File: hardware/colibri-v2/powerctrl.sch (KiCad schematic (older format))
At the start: 47 parts, among them CN1 XT60-M, CN2 XT60-F, CON1 BARREL_JACK, Q1 PDTC123JU, Q10 PDTC123JU, Q11 PDTA123JU, Q2 PDTA123JU, Q3 BSS138PW, Q4 FDMA530PZ, Q5 BSS138PW, Q6 BSS138PW, Q7 BSS138PW, Q8 AP6681GMT-HF-3TR, Q9 FDMA530PZ, SW10 B3F-1020, SW9 ALPS-SPPJ320600, T1 BATCHARGE+, T2 BATCHARGE-

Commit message: Adding and assigning footprints
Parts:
- Q3, Q5, Q6, Q7: footprint (none) -> TO_SOT_Packages_SMD:SOT-323
- Q4, Q9: footprint (none) -> Sigmadrone:FDMA530PZ
- SW10: value B3F-1020 -> OMRON B3F-1070; footprint (none) -> Sigmadrone:SW_TH_Tactile_Omron_B3F-10xx_6x6
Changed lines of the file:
@@
 F 0 "Q5" H 5600 2000 50  0000 R CNN
 F 1 "BSS138PW" H 5300 2150 50  0000 R CNN
-F 2 "" H 5500 2050 29  0001 C CNN
+F 2 "TO_SOT_Packages_SMD:SOT-323" H 5500 2050 29  0001 C CNN
 F 3 "" H 5300 1950 60  0000 C CNN
 	1    5300 1950
@@
 F 0 "Q9" H 7510 3260 50  0000 R CNN
 F 1 "FDMA530PZ" V 8000 3150 50  0000 R CNN
-F 2 "" H 7850 3250 29  0001 C CNN
+F 2 "Sigmadrone:FDMA530PZ" H 7850 3250 29  0001 C CNN
 F 3 "" H 7650 3150 60  0000 C CNN
 	1    7650 3150
@@
 F 0 "Q4" H 4060 3260 50  0000 R CNN
 F 1 "FDMA530PZ" V 4500 3150 50  0000 R CNN
-F 2 "" H 4400 3250 29  0001 C CNN
+F 2 "Sigmadrone:FDMA530PZ" H 4400 3250 29  0001 C CNN
 F 3 "" H 4200 3150 60  0000 C CNN
 	1    4200 3150
@@
 F 0 "Q6" H 6000 5050 50  0000 R CNN
 F 1 "BSS138PW" H 5700 5200 50  0000 R CNN
-F 2 "" H 5900 5100 29  0001 C CNN
+F 2 "TO_SOT_Packages_SMD:SOT-323" H 5900 5100 29  0001 C CNN
 F 3 "" H 5700 5000 60  0000 C CNN
 	1    5700 5000
@@
 F 0 "Q7" H 6650 5050 50  0000 R CNN
 F 1 "BSS138PW" H 6350 5200 50  0000 R CNN
-F 2 "" H 6550 5100 29  0001 C CNN
+F 2 "TO_SOT_Packages_SMD:SOT-323" H 6550 5100 29  0001 C CNN
 F 3 "" H 6350 5000 60  0000 C CNN
 	1    6350 5000
@@
 P 7750 5150
 F 0 "SW10" H 7900 5260 50  0000 C CNN
-F 1 "B3F-1020" H 7750 4950 50  0000 C CNN
-F 2 "" H 7750 5150 60  0001 C CNN
+F 1 "OMRON B3F-1070" H 7750 4950 50  0000 C CNN
+F 2 "Sigmadrone:SW_TH_Tactile_Omron_B3F-10xx_6x6" H 7750 5150 60  0001 C CNN
 F 3 "" H 7750 5150 60  0000 C CNN
 F 4 "1960939" H 7750 5150 60  0001 C CNN "Part"
@@
 F 0 "Q3" H 3750 6300 50  0000 R CNN
 F 1 "BSS138PW" H 3450 6450 50  0000 R CNN
-F 2 "" H 3650 6350 29  0001 C CNN
+F 2 "TO_SOT_Packages_SMD:SOT-323" H 3650 6350 29  0001 C CNN
 F 3 "" H 3450 6250 60  0000 C CNN
 	1    3450 6250

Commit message: Added footprints
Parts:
- removed D4: BZV55-C18, symbol ZENER
- removed Q1: PDTC123JU, TO_SOT_Packages_SMD:SOT-323, symbol RET_NPN_SMT
- removed Q2: PDTA123JU, TO_SOT_Packages_SMD:SOT-323, symbol RET_PNP_SMT
- added C125: 100nF/50V/X7R, Capacitors_SMD:C_0603, symbol C_SMT
- added U27: LTC4412, Sigmadrone:SOT23-6_LTC4412, symbol LTC4412
- D2: value D_Schottky -> VS-15MQ040NTRPBF; footprint (none) -> Sigmadrone:DO-214AC; Part (none) -> 1463215; Provider (none) -> Farnell
- D3, D8, D9: footprint (none) -> Diodes_SMD:SOD-323
- D5: footprint (none) -> Sigmadrone:DO-214AC
- D6, D7: footprint (none) -> Sigmadrone:SOD-80
- R43: value 10K/5% -> 100R/5%; Part 9331700 -> 9331689
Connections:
- wire segments 136 -> 138
- no-connect marks 0 -> 1

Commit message: Added Power Jack footprint
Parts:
- removed T1: BATCHARGE+, symbol 726386-2
- removed T2: BATCHARGE-, symbol 726386-2
- added CN12: XT60-F, Sigmadrone:xt60, symbol XT60
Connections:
- wire segments 138 -> 135
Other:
- moved on the sheet: C125, C26, C27, C28, C29, CN1, CN2, CON1, D2, D3, D5, D6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

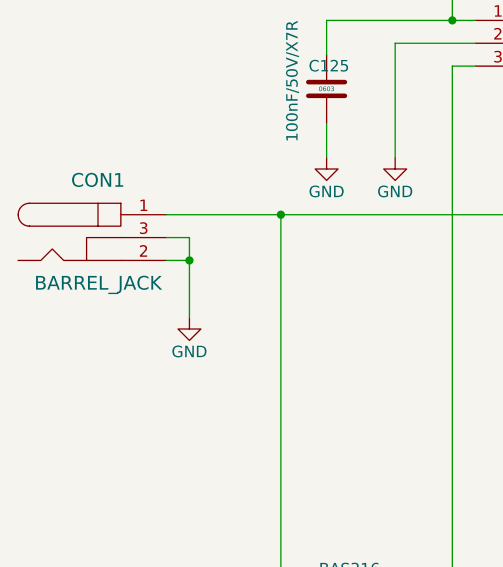
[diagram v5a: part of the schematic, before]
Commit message: Added footprints
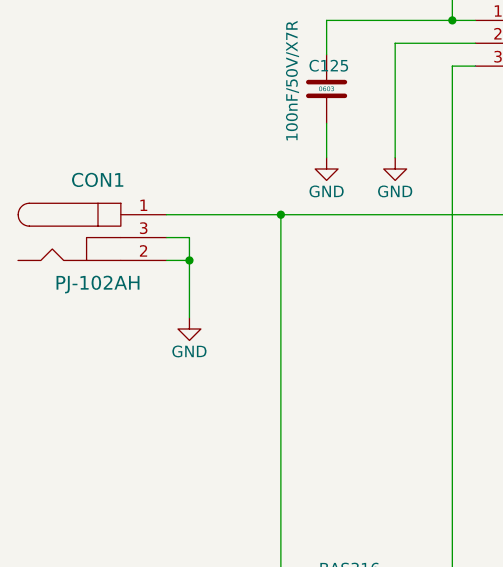
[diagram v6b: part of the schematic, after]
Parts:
- CON1: value BARREL_JACK -> PJ-102AH; footprint (none) -> Sigmadrone:PJ-102AH; Part (none) -> CP-102AH-ND; Provider (none) -> Digikey
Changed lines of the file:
@@
 $EndComp
 $Comp
-L +BATT #PWR49
+L +BATT #PWR051
 U 1 1 55962B26
 P 1650 950
-F 0 "#PWR49" H 1650 800 50  0001 C CNN
+F 0 "#PWR051" H 1650 800 50  0001 C CNN
 F 1 "+BATT" H 1650 1090 50  0000 C CNN
 F 2 "" H 1650 950 60  0000 C CNN
@@
 VH_CTRL
 $Comp
-L GND #PWR60
+L GND #PWR052
 U 1 1 55A491DA
 P 4850 2550
-F 0 "#PWR60" H 4850 2300 50  0001 C CNN
+F 0 "#PWR052" H 4850 2300 50  0001 C CNN
 F 1 "GND" H 4850 2400 50  0000 C CNN
 F 2 "" H 4850 2550 60  0000 C CNN
@@
 $EndComp
 $Comp
-L GND #PWR62
+L GND #PWR053
 U 1 1 55ADC831
 P 5400 2550
-F 0 "#PWR62" H 5400 2300 50  0001 C CNN
+F 0 "#PWR053" H 5400 2300 50  0001 C CNN
 F 1 "GND" H 5400 2400 50  0000 C CNN
 F 2 "" H 5400 2550 60  0000 C CNN
@@
 $EndComp
 $Comp
-L +BATT #PWR51
+L +BATT #PWR054
 U 1 1 55ADD6AC
 P 1650 3000
-F 0 "#PWR51" H 1650 2850 50  0001 C CNN
+F 0 "#PWR054" H 1650 2850 50  0001 C CNN
 F 1 "+BATT" H 1650 3140 50  0000 C CNN
 F 2 "" H 1650 3000 60  0000 C CNN
@@
 P 1000 4850
 F 0 "CON1" H 1000 5100 60  0000 C CNN
-F 1 "BARREL_JACK" H 1000 4650 60  0000 C CNN
-F 2 "" H 1000 4850 60  0001 C CNN
+F 1 "PJ-102AH" H 1000 4650 60  0000 C CNN
+F 2 "Sigmadrone:PJ-102AH" H 1000 4850 60  0001 C CNN
 F 3 "" H 1000 4850 60  0000 C CNN
+F 4 "CP-102AH-ND" H 1000 4850 60  0001 C CNN "Part"
+F 5 "Digikey" H 1000 4850 60  0001 C CNN "Provider"
 	1    1000 4850
 	1    0    0    -1
@@
 $EndComp
 $Comp
-L GND #PWR59
+L GND #PWR055
 U 1 1 564AD1EF
 P 3700 4450
-F 0 "#PWR59" H 3700 4200 50  0001 C CNN
+F 0 "#PWR055" H 3700 4200 50  0001 C CNN
 F 1 "GND" H 3700 4300 50  0000 C CNN
 F 2 "" H 3700 4450 60  0000 C CNN
@@
 $EndComp
 $Comp
-L GND #PWR65
+L GND #PWR056
 U 1 1 565060C5
 P 5800 5800
-F 0 "#PWR65" H 5800 5550 50  0001 C CNN
+F 0 "#PWR056" H 5800 5550 50  0001 C CNN
 F 1 "GND" H 5800 5650 50  0000 C CNN
 F 2 "" H 5800 5800 60  0000 C CNN
@@
 $EndComp
 $Comp
-L GND #PWR66
+L GND #PWR057
 U 1 1 565061BE
 P 6250 5800
-F 0 "#PWR66" H 6250 5550 50  0001 C CNN
+F 0 "#PWR057" H 6250 5550 50  0001 C CNN
 F 1 "GND" H 6250 5650 50  0000 C CNN
 F 2 "" H 6250 5800 60  0000 C CNN
@@
 $EndComp
 $Comp
-L GND #PWR67
+L GND #PWR058
 U 1 1 565065E3
 P 6650 5800
-F 0 "#PWR67" H 6650 5550 50  0001 C CNN
+F 0 "#PWR058" H 6650 5550 50  0001 C CNN
 F 1 "GND" H 6650 5650 50  0000 C CNN
 F 2 "" H 6650 5800 60  0000 C CNN
@@
 $EndComp
 $Comp
-L GND #PWR63
+L GND #PWR059
 U 1 1 56507987
 P 5400 5800
-F 0 "#PWR63" H 5400 5550 50  0001 C CNN
+F 0 "#PWR059" H 5400 5550 50  0001 C CNN
 F 1 "GND" H 5400 5650 50  0000 C CNN
 F 2 "" H 5400 5800 60  0000 C CNN
@@
 $EndComp
 $Comp
-L GND #PWR68
+L GND #PWR060
 U 1 1 5650962F
 P 7650 5800
-F 0 "#PWR68" H 7650 5550 50  0001 C CNN
+F 0 "#PWR060" H 7650 5550 50  0001 C CNN
 F 1 "GND" H 7650 5650 50  0000 C CNN
 F 2 "" H 7650 5800 60  0000 C CNN
@@
 $EndComp
 $Comp
-L +3V3 #PWR72
+L +3V3 #PWR061
 U 1 1 5650D441
 P 8800 4200
-F 0 "#PWR72" H 8800 4050 50  0001 C CNN
+F 0 "#PWR061" H 8800 4050 50  0001 C CNN
 F 1 "+3V3" H 8800 4340 50  0000 C CNN
 F 2 "" H 8800 4200 60  0000 C CNN
@@
 $EndComp
 $Comp
-L GND #PWR69
+L GND #PWR062
 U 1 1 5650DE62
 P 8200 3850
-F 0 "#PWR69" H 8200 3600 50  0001 C CNN
+F 0 "#PWR062" H 8200 3600 50  0001 C CNN
 F 1 "GND" H 8200 3700 50  0000 C CNN
 F 2 "" H 8200 3850 60  0000 C CNN
@@
 $EndComp
 $Comp
-L GND #PWR58
+L GND #PWR063
 U 1 1 5650ECED
 P 3550 7450
-F 0 "#PWR58" H 3550 7200 50  0001 C CNN
+F 0 "#PWR063" H 3550 7200 50  0001 C CNN
 F 1 "GND" H 3550 7300 50  0000 C CNN
 F 2 "" H 3550 7450 60  0000 C CNN
@@
 $EndComp
 $Comp
-L GND #PWR56
+L GND #PWR064
 U 1 1 5650ECF4
 P 3150 7450
-F 0 "#PWR56" H 3150 7200 50  0001 C CNN
+F 0 "#PWR064" H 3150 7200 50  0001 C CNN
 F 1 "GND" H 3150 7300 50  0000 C CNN
 F 2 "" H 3150 7450 60  0000 C CNN
@@
 $EndComp
 $Comp
-L +3V3 #PWR57
+L +3V3 #PWR065
 U 1 1 5650F275
 P 3550 5600
-F 0 "#PWR57" H 3550 5450 50  0001 C CNN
+F 0 "#PWR065" H 3550 5450 50  0001 C CNN
 F 1 "+3V3" H 3550 5740 50  0000 C CNN
 F 2 "" H 3550 5600 60  0000 C CNN
@@
 JTAG_PWR_ON
 $Comp
-L GND #PWR54
+L GND #PWR066
 U 1 1 56510E0B
 P 2300 4500
-F 0 "#PWR54" H 2300 4250 50  0001 C CNN
+F 0 "#PWR066" H 2300 4250 50  0001 C CNN
 F 1 "GND" H 2300 4350 50  0000 C CNN
 F 2 "" H 2300 4500 60  0000 C CNN
@@
 $EndComp
 $Comp
-L GND #PWR61
+L GND #PWR067
 U 1 1 5651137E
 P 5150 4000
-F 0 "#PWR61" H 5150 3750 50  0001 C CNN
+F 0 "#PWR067" H 5150 3750 50  0001 C CNN
 F 1 "GND" H 5150 3850 50  0000 C CNN
 F 2 "" H 5150 4000 60  0000 C CNN
@@
 $EndComp
 $Comp
-L GND #PWR64
+L GND #PWR068
 U 1 1 56511422
 P 5550 4000
-F 0 "#PWR64" H 5550 3750 50  0001 C CNN
+F 0 "#PWR068" H 5550 3750 50  0001 C CNN
 F 1 "GND" H 5550 3850 50  0000 C CNN
 F 2 "" H 5550 4000 60  0000 C CNN
@@
 $EndComp
 $Comp
-L GND #PWR50
+L GND #PWR069
 U 1 1 5651558E
 P 1650 1650
-F 0 "#PWR50" H 1650 1400 50  0001 C CNN
+F 0 "#PWR069" H 1650 1400 50  0001 C CNN
 F 1 "GND" H 1650 1500 50  0000 C CNN
 F 2 "" H 1650 1650 60  0000 C CNN
@@
 $EndComp
 $Comp
-L GND #PWR71
+L GND #PWR070
 U 1 1 56515698
 P 8250 1650
-F 0 "#PWR71" H 8250 1400 50  0001 C CNN
+F 0 "#PWR070" H 8250 1400 50  0001 C CNN
 F 1 "GND" H 8250 1500 50  0000 C CNN
 F 2 "" H 8250 1650 60  0000 C CNN
@@
 $EndComp
 $Comp
-L GND #PWR48
+L GND #PWR071
 U 1 1 5651D821
 P 1400 5200
-F 0 "#PWR48" H 1400 4950 50  0001 C CNN
+F 0 "#PWR071" H 1400 4950 50  0001 C CNN
 F 1 "GND" H 1400 5050 50  0000 C CNN
 F 2 "" H 1400 5200 60  0000 C CNN
@@
 $EndComp
 $Comp
-L GND #PWR52
+L GND #PWR072
 U 1 1 56520674
 P 1800 7450
-F 0 "#PWR52" H 1800 7200 50  0001 C CNN
+F 0 "#PWR072" H 1800 7200 50  0001 C CNN
 F 1 "GND" H 1800 7300 50  0000 C CNN
 F 2 "" H 1800 7450 60  0000 C CNN
@@
 $EndComp
 $Comp
-L GND #PWR75
+L GND #PWR073
 U 1 1 56522BEE
 P 9700 2600
-F 0 "#PWR75" H 9700 2350 50  0001 C CNN
+F 0 "#PWR073" H 9700 2350 50  0001 C CNN
 F 1 "GND" H 9700 2450 50  0000 C CNN
 F 2 "" H 9700 2600 60  0000 C CNN
@@
 $EndComp
 $Comp
-L +BATT #PWR74
+L +BATT #PWR074
 U 1 1 56523199
 P 9700 1450
-F 0 "#PWR74" H 9700 1300 50  0001 C CNN
+F 0 "#PWR074" H 9700 1300 50  0001 C CNN
 F 1 "+BATT" H 9700 1590 50  0000 C CNN
 F 2 "" H 9700 1450 60  0000 C CNN
@@
 $EndComp
 $Comp
-L GND #PWR73
+L GND #PWR075
 U 1 1 56523CCD
 P 9300 2600
-F 0 "#PWR73" H 9300 2350 50  0001 C CNN
+F 0 "#PWR075" H 9300 2350 50  0001 C CNN
 F 1 "GND" H 9300 2450 50  0000 C CNN
 F 2 "" H 9300 2600 60  0000 C CNN
@@
 $EndComp
 $Comp
-L GND #PWR76
+L GND #PWR076
 U 1 1 56524360
 P 10100 2600
-F 0 "#PWR76" H 10100 2350 50  0001 C CNN
+F 0 "#PWR076" H 10100 2350 50  0001 C CNN
 F 1 "GND" H 10100 2450 50  0000 C CNN
 F 2 "" H 10100 2600 60  0000 C CNN
@@
 $EndComp
 $Comp
-L VH #PWR70
+L VH #PWR077
 U 1 1 56C841E3
 P 8250 950
-F 0 "#PWR70" H 8250 800 50  0001 C CNN
+F 0 "#PWR077" H 8250 800 50  0001 C CNN
 F 1 "VH" H 8268 1124 50  0000 C CNN
 F 2 "" H 8250 950 50  0000 C CNN
@@
 $EndComp
 $Comp
-L PWR_FLAG #FLG4
+L PWR_FLAG #FLG078
 U 1 1 56CCA634
 P 2050 950
-F 0 "#FLG4" H 2050 1045 50  0001 C CNN
+F 0 "#FLG078" H 2050 1045 50  0001 C CNN
 F 1 "PWR_FLAG" H 2050 1174 50  0000 C CNN
 F 2 "" H 2050 950 50  0000 C CNN
@@
 $EndComp
 $Comp
-L PWR_FLAG #FLG6
+L PWR_FLAG #FLG079
 U 1 1 56CCD628
 P 7950 950
-F 0 "#FLG6" H 7950 1045 50  0001 C CNN
+F 0 "#FLG079" H 7950 1045 50  0001 C CNN
 F 1 "PWR_FLAG" H 7950 1174 50  0000 C CNN
 F 2 "" H 7950 950 50  0000 C CNN
@@
 $EndComp
 $Comp
-L PWR_FLAG #FLG7
+L PWR_FLAG #FLG080
 U 1 1 56CD26EC
 P 8200 2800
-F 0 "#FLG7" H 8200 2895 50  0001 C CNN
+F 0 "#FLG080" H 8200 2895 50  0001 C CNN
 F 1 "PWR_FLAG" H 8200 3024 50  0000 C CNN
 F 2 "" H 8200 2800 50  0000 C CNN
@@
 $EndComp
 $Comp
-L GND #PWR53
+L GND #PWR081
 U 1 1 56D1869D
 P 2000 4500
-F 0 "#PWR53" H 2000 4250 50  0001 C CNN
+F 0 "#PWR081" H 2000 4250 50  0001 C CNN
 F 1 "GND" H 2000 4350 50  0000 C CNN
 F 2 "" H 2000 4500 60  0000 C CNN
@@
 Connection ~ 2550 3200
 $Comp
-L PWR_FLAG #FLG5
+L PWR_FLAG #FLG082
 U 1 1 56D35731
 P 2550 2850
-F 0 "#FLG5" H 2550 2945 50  0001 C CNN
+F 0 "#FLG082" H 2550 2945 50  0001 C CNN
 F 1 "PWR_FLAG" H 2550 3030 50  0000 C CNN
 F 2 "" H 2550 2850 50  0000 C CNN
@@
 Connection ~ 2800 1200
 $Comp
-L GND #PWR55
+L GND #PWR083
 U 1 1 56D660D5
 P 3050 1700
-F 0 "#PWR55" H 3050 1450 50  0001 C CNN
+F 0 "#PWR083" H 3050 1450 50  0001 C CNN
 F 1 "GND" H 3050 1550 50  0000 C CNN
 F 2 "" H 3050 1700 60  0000 C CNN

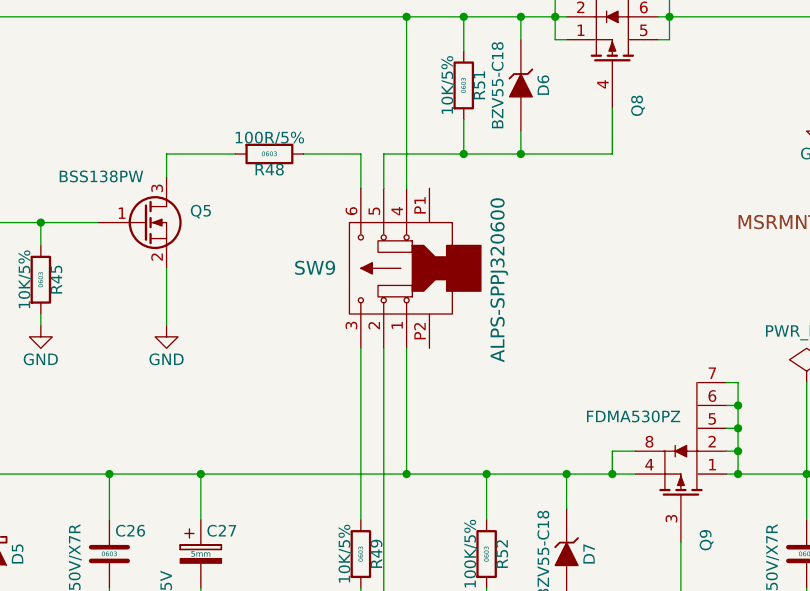
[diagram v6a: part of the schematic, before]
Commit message: Added SPPJ320600.kicad_mod
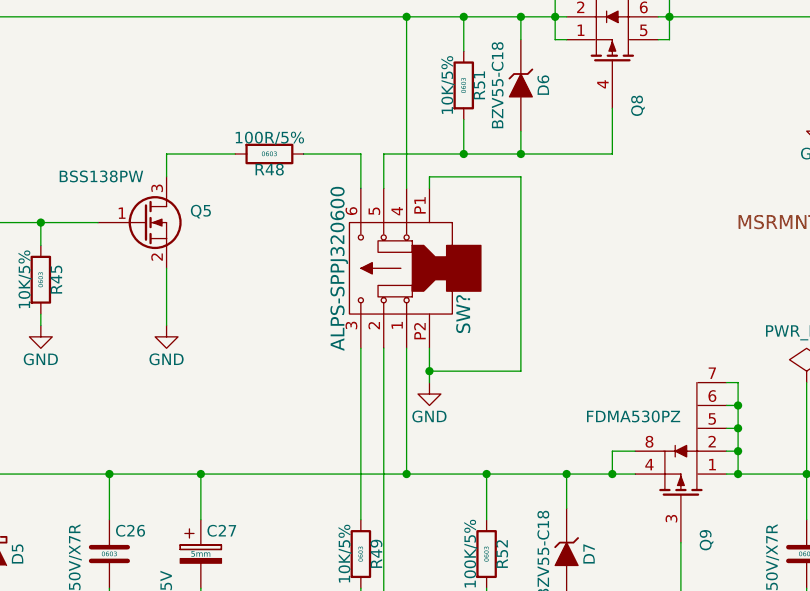
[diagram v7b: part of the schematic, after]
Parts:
- removed SW9: ALPS-SPPJ320600, symbol ALPS-SPPJ320600
- added SW?: ALPS-SPPJ320600, symbol ALPS-SPPJ320600
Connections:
- net +BATT: now also SW?.4
- net GND: now also SW?.P1, SW?.P2
- net at D6.2 (A), Q8.4 (G), R51.2: now also SW?.5
- net at C26.1, C27.1, D5.1 (K)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: now also SW?.1
- net at D7.2 (A), Q9.3 (G), R52.2: now also SW?.2
- net at R49.1: now also SW?.3
- net at R48.1: now also SW?.6

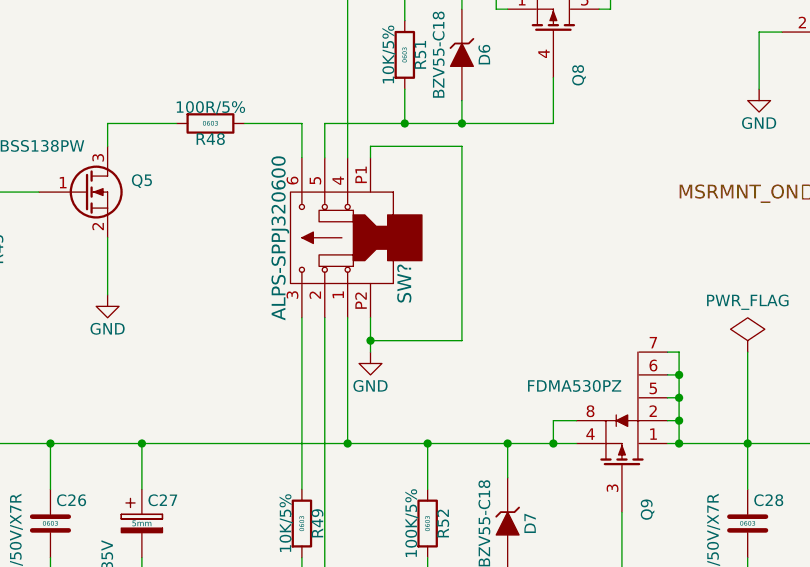
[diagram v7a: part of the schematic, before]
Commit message: Added VL_1220.kicad_mod footprint
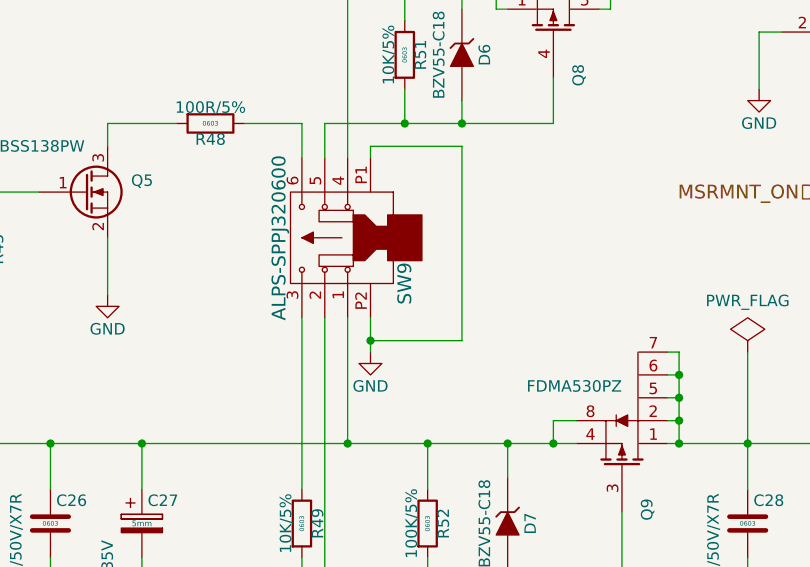
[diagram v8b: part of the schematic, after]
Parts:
- removed SW?: ALPS-SPPJ320600, symbol ALPS-SPPJ320600
- added SW9: ALPS-SPPJ320600, Sigmadrone:SPPJ320600, symbol ALPS-SPPJ320600
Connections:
- net +BATT: now also SW9.4
- net GND: now also SW9.P1, SW9.P2
- net at D6.2 (A), Q8.4 (G), R51.2: now also SW9.5
- net at C26.1, C27.1, D5.1 (K)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: now also SW9.1
- net at D7.2 (A), Q9.3 (G), R52.2: now also SW9.2
- net at R48.1: now also SW9.6
- net at R49.1: now also SW9.3
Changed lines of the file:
@@
 $EndComp
 $Comp
-L ALPS-SPPJ320600 SW?
-U 1 1 56D8D0EF
-P 6300 2300
-F 0 "SW?" H 6500 2700 60  0000 C CNN
-F 1 "ALPS-SPPJ320600" H 6300 2150 60  0000 C CNN
-F 2 "" H 6300 2300 60  0000 C CNN
-F 3 "" H 6300 2300 60  0000 C CNN
-	1    6300 2300
-	0    1    1    0
-$EndComp
-$Comp
-L GND #PWR?
+L GND #PWR084
 U 1 1 56D8D269
 P 6550 2800
-F 0 "#PWR?" H 6550 2550 50  0001 C CNN
+F 0 "#PWR084" H 6550 2550 50  0001 C CNN
 F 1 "GND" H 6550 2650 50  0000 C CNN
 F 2 "" H 6550 2800 50  0000 C CNN
@@
 	6950 2750 6550 2750
 Connection ~ 6550 2750
+$Comp
+L ALPS-SPPJ320600 SW9
+U 1 1 56D7E87C
+P 6300 2300
+F 0 "SW9" H 6500 2700 60  0000 C CNN
+F 1 "ALPS-SPPJ320600" H 6300 2150 60  0000 C CNN
+F 2 "Sigmadrone:SPPJ320600" H 6400 2600 60  0001 C CNN
+F 3 "" H 6500 2700 60  0000 C CNN
+F 4 "688-SPPJ320600" H 6600 2800 60  0001 C CNN "Part"
+F 5 "Mouser" H 6700 2900 60  0001 C CNN "Provider"
+	1    6300 2300
+	0    1    1    0
+$EndComp
 $EndSCHEMATC
